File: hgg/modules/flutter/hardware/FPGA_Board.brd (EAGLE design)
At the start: 100 x 77 mm, 87 parts, among them IC1 AT45DB161D-SU, IC2 MEGA8-AI, IC3 MAX481CSA, Q1 8Mhz, U2 XC3S50AVQ100, X1 BU-SMA-V, X2 MINI-USB-32005-201

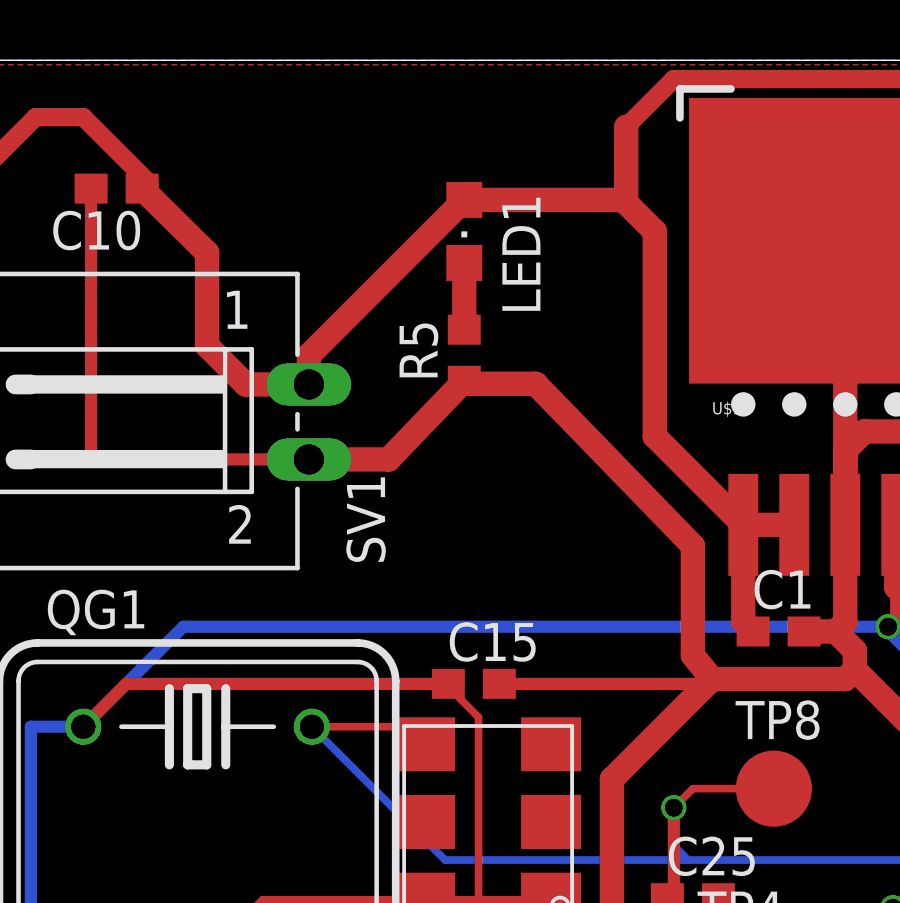
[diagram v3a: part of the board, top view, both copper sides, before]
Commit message: flutter pcb is ready for review
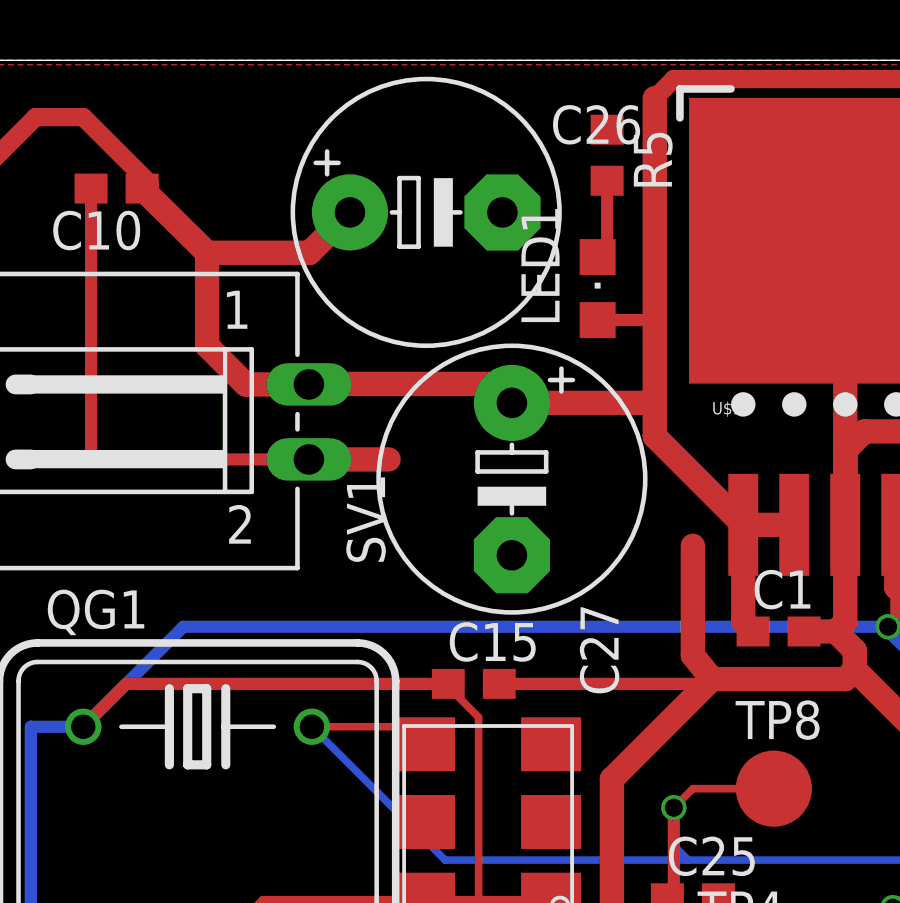
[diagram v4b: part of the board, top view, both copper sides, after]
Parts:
- added C26, C27: (no value), resistor:E5-8,5
- moved R5 8.19 mm to (23.5, 76.8), turned to 270 degrees
- moved LED1 4.84 mm to (23.2, 72.4), turned to 0 degrees
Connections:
- net +5V: now also C26.+, C27.+
- net GND: now also C26.-, C27.-
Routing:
- net GND: track 718.4 -> 704.7 mm
- net +5V: track 294.9 -> 299.8 mm
- net N$3: track 2.23 -> 2.86 mm
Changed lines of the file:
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@@
 <element name="C2" library="resistor" package="C0603" value="100n" x="51.1175" y="61.2775"/>
 <element name="C3" library="resistor" package="C0603" value="100n" x="70.1675" y="61.2775"/>
-<element name="LED1" library="led" package="CHIPLED_0805" value="" x="18.7325" y="74.295" rot="R180"/>
-<element name="R5" library="resistor" package="R0603" value="470" x="18.7325" y="70.1675" rot="R90"/>
+<element name="LED1" library="led" package="CHIPLED_0805" value="" x="23.1775" y="72.39"/>
+<element name="R5" library="resistor" package="R0603" value="470" x="23.495" y="76.835" rot="R270"/>
 <element name="C4" library="resistor" package="C0603" value="100n" x="39.6875" y="66.04" rot="R180"/>
 <element name="C5" library="resistor" package="C0603" value="100n" x="60.6425" y="66.3575"/>
@@
 <element name="R16" library="resistor" package="R0603" value="1k" x="71.12" y="14.2875" rot="R180"/>
 <element name="R17" library="resistor" package="R0603" value="1.6k" x="76.5175" y="16.1925"/>
+<element name="C26" library="resistor" package="E5-8,5" value="" x="17.4625" y="74.93"/>
+<element name="C27" library="resistor" package="E5-8,5" value="" x="20.32" y="66.04" rot="R270"/>
 </elements>
 <signals>
@@
 <wire x1="31.115" y1="21.59" x2="33.655" y2="21.59" width="0.254" layer="16"/>
 <wire x1="13.5525" y1="66.695" x2="16.21" y2="66.695" width="0.8128" layer="1"/>
-<wire x1="16.21" y1="66.695" x2="18.7325" y2="69.3175" width="0.8128" layer="1"/>
 <wire x1="30.06" y1="60.96" x2="31.115" y2="60.96" width="0.8128" layer="1"/>
 <wire x1="31.115" y1="60.96" x2="31.4325" y2="61.2775" width="0.8128" layer="1"/>
 <wire x1="31.4325" y1="61.2775" x2="31.4325" y2="64.515" width="0.8128" layer="1"/>
-<wire x1="18.7325" y1="69.3175" x2="18.7325" y2="69.37375" width="0.8128" layer="1"/>
-<wire x1="18.7325" y1="69.3175" x2="18.7325" y2="69.2175" width="0.8128" layer="1"/>
-<wire x1="18.7325" y1="69.2175" x2="21.11125" y2="69.2175" width="0.8128" layer="1"/>
-<wire x1="21.11125" y1="69.2175" x2="26.3525" y2="63.8175" width="0.8128" layer="1"/>
 <wire x1="26.3525" y1="63.8175" x2="26.3525" y2="60.16625" width="0.8128" layer="1"/>
 <wire x1="26.3525" y1="60.16625" x2="26.9875" y2="59.3725" width="0.8128" layer="1"/>
@@
 <via x="54.2925" y="8.5725" extent="1-16" drill="0.6" shape="octagon"/>
 <wire x1="54.2925" y1="8.5725" x2="53.5" y2="8.5725" width="0.254" layer="1"/>
+<contactref element="C26" pad="-"/>
+<contactref element="C27" pad="-"/>
 <wire x1="76.5" y1="0.6525" x2="76.5" y2="0.74" width="0" layer="19" extent="16-16"/>
 <wire x1="73.5" y1="0.74" x2="73.50125" y2="0.74125" width="0" layer="19" extent="16-16"/>
@@
 <wire x1="10.16" y1="70.485" x2="10.16" y2="73.585" width="0.8128" layer="1"/>
 <wire x1="10.16" y1="73.585" x2="7.99375" y2="75.72375" width="0.8128" layer="1"/>
-<wire x1="13.5525" y1="69.195" x2="13.5525" y2="70.165" width="0.8128" layer="1"/>
-<wire x1="13.5525" y1="70.165" x2="18.7325" y2="75.345" width="0.8128" layer="1"/>
-<wire x1="18.7325" y1="75.345" x2="24.0325" y2="75.345" width="0.8128" layer="1"/>
-<wire x1="24.0325" y1="75.345" x2="24.13" y2="75.2475" width="0.8128" layer="1"/>
-<wire x1="25.0825" y1="74.295" x2="25.0825" y2="67.465" width="0.8128" layer="1"/>
+<wire x1="13.5525" y1="69.195" x2="13.5525" y2="69.2125" width="0.8128" layer="1"/>
+<wire x1="25.0825" y1="78.74" x2="25.0825" y2="71.4375" width="0.8128" layer="1"/>
+<wire x1="25.0825" y1="71.4375" x2="25.0825" y2="68.58" width="0.8128" layer="1"/>
+<wire x1="25.0825" y1="68.58" x2="25.0825" y2="67.465" width="0.8128" layer="1"/>
 <wire x1="25.0825" y1="67.465" x2="28.0325" y2="64.515" width="0.8128" layer="1"/>
 <wire x1="28.0325" y1="64.515" x2="28.0325" y2="61.2875" width="0.8128" layer="1"/>
@@
 <wire x1="44.29125" y1="79.21625" x2="44.1325" y2="79.375" width="0.6096" layer="1"/>
 <wire x1="44.1325" y1="79.375" x2="25.7175" y2="79.375" width="0.6096" layer="1"/>
-<wire x1="25.7175" y1="79.375" x2="24.13" y2="77.7875" width="0.6096" layer="1"/>
-<wire x1="24.13" y1="77.7875" x2="24.13" y2="75.2475" width="0.8128" layer="1"/>
-<wire x1="24.13" y1="75.2475" x2="25.0825" y2="74.295" width="0.8128" layer="1"/>
+<wire x1="25.7175" y1="79.375" x2="25.0825" y2="78.74" width="0.6096" layer="1"/>
 <wire x1="48.3525" y1="64.515" x2="50.0525" y2="64.515" width="0.8128" layer="1"/>
 <wire x1="50.2675" y1="61.2775" x2="50.2675" y2="64.3" width="0.8128" layer="1"/>
@@
 <wire x1="66.3575" y1="11.1125" x2="66.675" y2="10.795" width="0.254" layer="1"/>
 <wire x1="66.675" y1="10.795" x2="66.675" y2="9.15035" width="0.254" layer="1"/>
+<contactref element="C27" pad="+"/>
+<contactref element="C26" pad="+"/>
+<wire x1="13.5525" y1="69.2125" x2="20.32" y2="69.2125" width="0.8128" layer="1"/>
+<wire x1="20.32" y1="69.2125" x2="20.32" y2="68.58" width="0.8128" layer="1"/>
+<wire x1="20.32" y1="68.58" x2="25.0825" y2="68.58" width="0.8128" layer="1"/>
+<wire x1="23.1775" y1="71.34" x2="25.0825" y2="71.34" width="0.4064" layer="1"/>
+<wire x1="25.0825" y1="71.34" x2="25.0825" y2="71.4375" width="0.4064" layer="1"/>
+<wire x1="10.16" y1="73.585" x2="13.5775" y2="73.585" width="0.8128" layer="1"/>
+<wire x1="13.5775" y1="73.585" x2="14.9225" y2="74.93" width="0.8128" layer="1"/>
 </signal>
 <signal name="VCC3.3">
@@
 <contactref element="LED1" pad="C"/>
 <contactref element="R5" pad="2"/>
-<wire x1="18.7325" y1="71.0175" x2="18.7325" y2="73.245" width="0.8128" layer="1"/>
+<wire x1="23.1775" y1="73.44" x2="23.495" y2="73.44" width="0.4064" layer="1"/>
+<wire x1="23.495" y1="73.44" x2="23.495" y2="75.985" width="0.4064" layer="1"/>
 </signal>
 <signal name="N$1">
